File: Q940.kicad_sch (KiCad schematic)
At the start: 15 parts, among them J1 Power, J101 TO_HX711, J102 SHT-3x Temperature-1, J103 SHT-3x Temperature-2, J104 TO L298N MOTOR-DRIVER, J105 I2C LCD 16x2, J106 PWR_INPUT, J2 Digital/PWM, J3 Analog, J4 Digital/PWM

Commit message: とりあえずリリース
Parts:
- added C106: 0.1uF/50V, Capacitor_THT:C_Disc_D3.8mm_W2.6mm_P2.50mm, symbol Device:C_Small
- added D101: 1N4007, symbol Device:D_Filled
- added M101: Geared Motor_DC 5V/5rpm, symbol Motor:Motor_DC
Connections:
- net +5V: now also C106.1, D101.1 (K), M101.1 (+)
- net GND: now also C106.2, D101.2 (A), M101.2 (-)

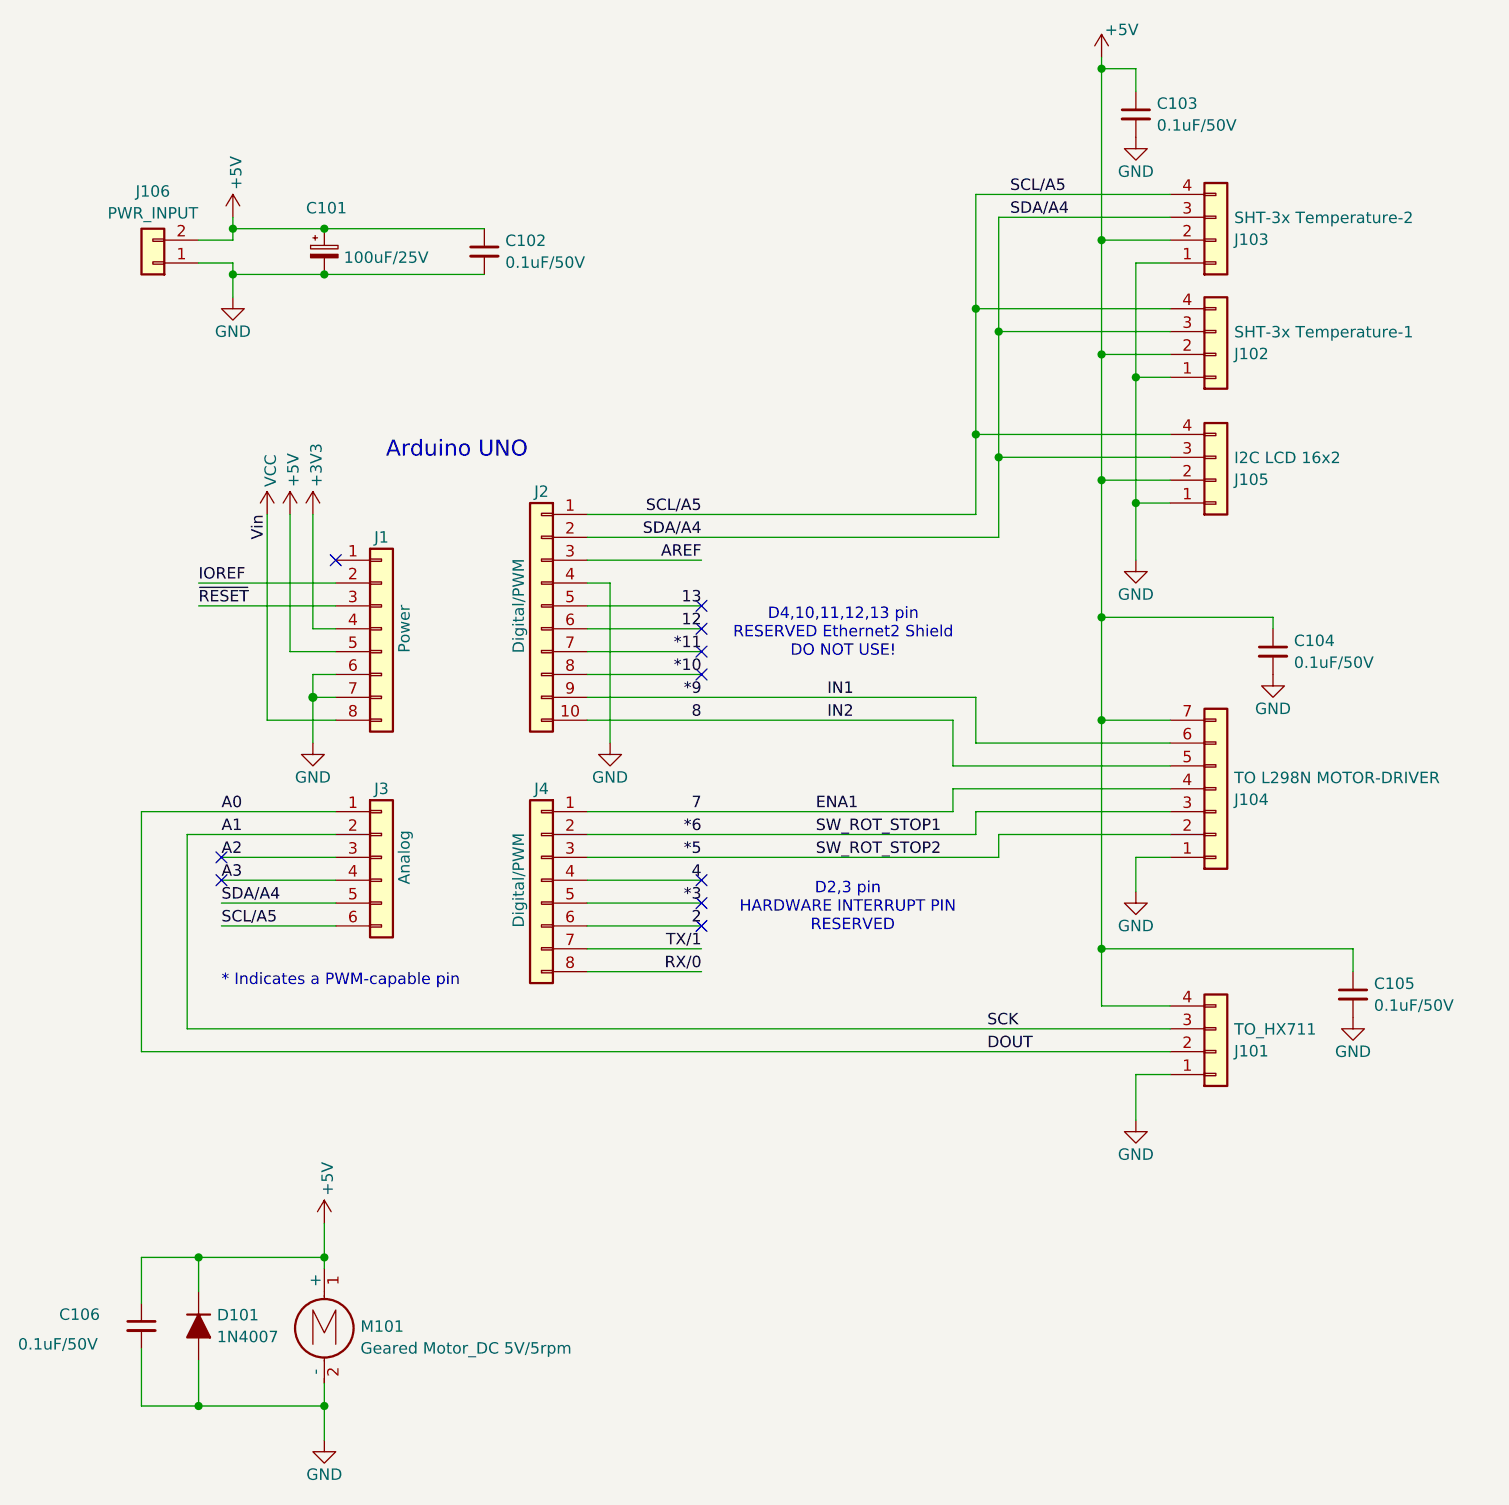
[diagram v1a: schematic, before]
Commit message: append MPU6050 and Hardware interruption
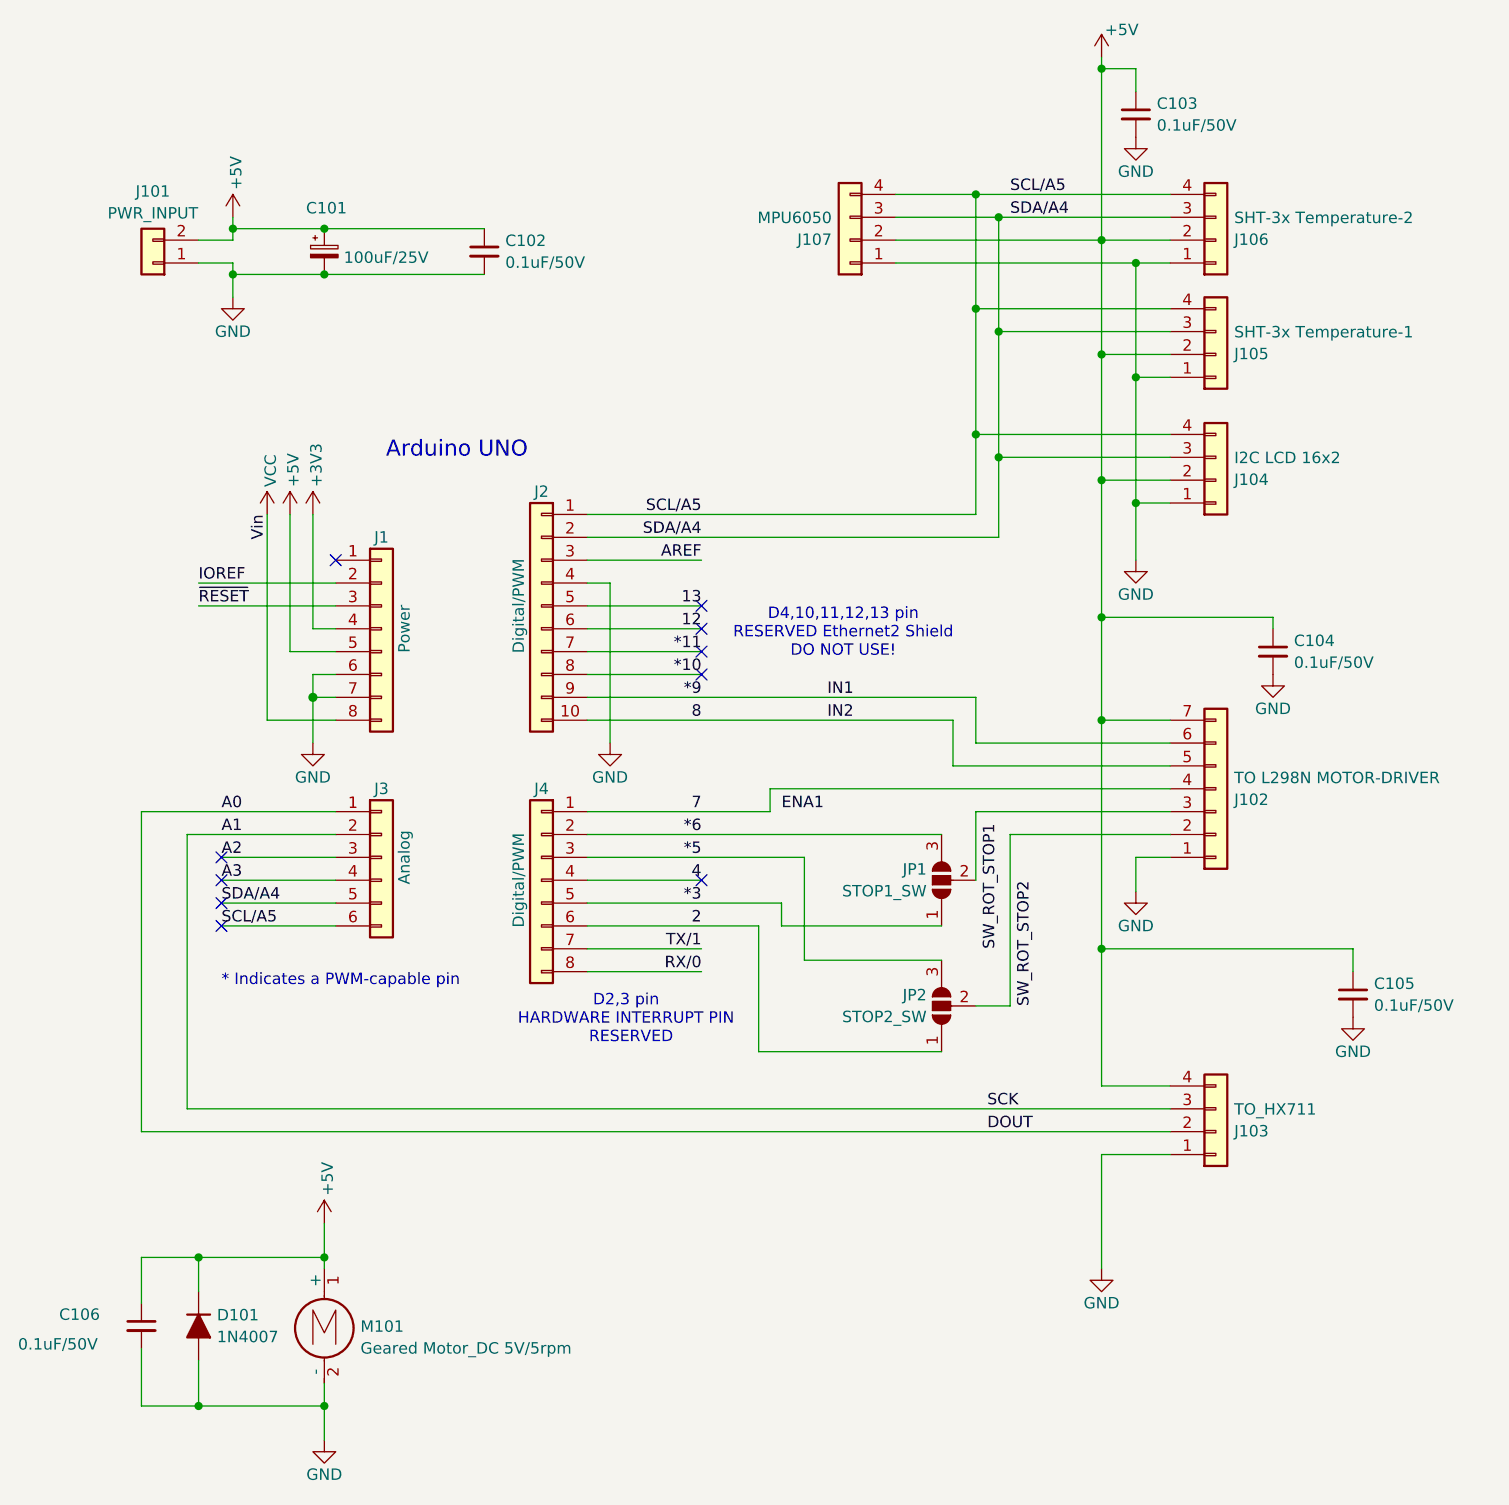
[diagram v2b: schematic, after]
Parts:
- added J107: MPU6050, Connector_JST:JST_XH_B4B-XH-A_1x04_P2.50mm_Vertical, symbol Connector_Generic:Conn_01x04
- added JP1: STOP1_SW, Jumper:SolderJumper-3_P1.3mm_Open_RoundedPad1.0x1.5mm_NumberLabels, symbol Jumper:SolderJumper_3_Open
- added JP2: STOP2_SW, Jumper:SolderJumper-3_P1.3mm_Open_RoundedPad1.0x1.5mm_NumberLabels, symbol Jumper:SolderJumper_3_Open
- J101: renamed from J106; footprint Connector_JST:JST_XH_B2B-XH-AM_1x02_P2.50mm_Vertical -> Connector_JST:JST_XH_B2B-XH-A_1x02_P2.50mm_Vertical
- J102: renamed from J104; footprint Connector_JST:JST_XH_B7B-XH-AM_1x07_P2.50mm_Vertical -> Connector_JST:JST_XH_B7B-XH-A_1x07_P2.50mm_Vertical
- J103: renamed from J101; footprint Connector_JST:JST_XH_B4B-XH-AM_1x04_P2.50mm_Vertical -> Connector_JST:JST_XH_B4B-XH-A_1x04_P2.50mm_Vertical
- J104: renamed from J105; footprint Connector_JST:JST_XH_B4B-XH-AM_1x04_P2.50mm_Vertical -> Connector_JST:JST_XH_B4B-XH-A_1x04_P2.50mm_Vertical
- J105: renamed from J102; footprint Connector_JST:JST_XH_B4B-XH-AM_1x04_P2.50mm_Vertical -> Connector_JST:JST_XH_B4B-XH-A_1x04_P2.50mm_Vertical
- J106: renamed from J103; footprint Connector_JST:JST_XH_B4B-XH-AM_1x04_P2.50mm_Vertical -> Connector_JST:JST_XH_B4B-XH-A_1x04_P2.50mm_Vertical
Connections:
- net *3: now also JP1.1 (A)
- net *5: now also JP2.3 (B); no longer J102.2 (Pin_2)
- net *6: now also JP1.3 (B); no longer J102.3 (Pin_3)
- net +5V: now also J107.2 (Pin_2)
- net 2: now also JP2.1 (A)
- net GND: now also J107.1 (Pin_1)
- net SCL/A5: now also J107.4 (Pin_4)
- net SDA/A4: now also J107.3 (Pin_3)
- new net: J102.2 (Pin_2), JP2.2 (C)
- new net: J102.3 (Pin_3), JP1.2 (C)
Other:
- moved on the sheet: J103

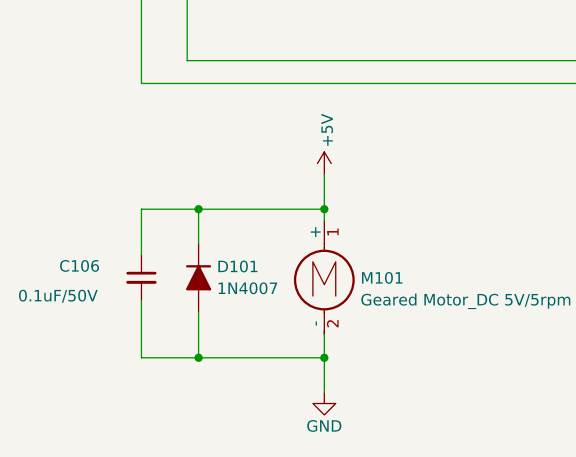
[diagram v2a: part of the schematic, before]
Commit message: remove 1N4007
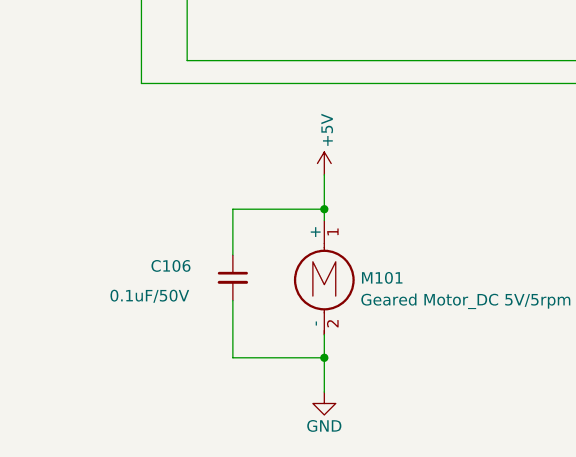
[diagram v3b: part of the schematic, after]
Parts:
- removed D101: 1N4007, symbol Device:D_Filled
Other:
- moved on the sheet: C106
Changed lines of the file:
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@@
-	)
-	(junction
-		(at 107.95 170.18)
-		(diameter 0)
-		(color 0 0 0 0)
 	)
 	(junction
@@
 	)
 	(junction
-		(at 107.95 153.67)
-		(diameter 0)
-		(color 0 0 0 0)
-	)
-	(junction
 		(at 208.28 40.64)
 		(diameter 0)
@@
 	(wire
 		(pts
-			(xy 107.95 153.67) (xy 121.92 153.67)
+			(xy 111.76 153.67) (xy 121.92 153.67)
 		)
 		(stroke
@@
 	(wire
 		(pts
-			(xy 107.95 153.67) (xy 101.6 153.67)
-		)
-		(stroke
-			(width 0)
-			(type default)
-		)
-	)
-	(wire
-		(pts
 			(xy 151.13 81.28) (xy 163.83 81.28)
 		)
@@
 	(wire
 		(pts
-			(xy 107.95 157.48) (xy 107.95 153.67)
-		)
-		(stroke
-			(width 0)
-			(type default)
-		)
-	)
-	(wire
-		(pts
 			(xy 190.5 120.65) (xy 175.26 120.65)
 		)
@@
 	(wire
 		(pts
-			(xy 107.95 165.1) (xy 107.95 170.18)
-		)
-		(stroke
-			(width 0)
-			(type default)
-		)
-	)
-	(wire
-		(pts
 			(xy 198.12 106.68) (xy 215.9 106.68)
 		)
@@
 	(wire
 		(pts
-			(xy 101.6 163.83) (xy 101.6 170.18)
+			(xy 111.76 163.83) (xy 111.76 170.18)
 		)
 		(stroke
@@
 	(wire
 		(pts
-			(xy 101.6 153.67) (xy 101.6 158.75)
+			(xy 111.76 153.67) (xy 111.76 158.75)
 		)
 		(stroke
@@
 	(wire
 		(pts
-			(xy 107.95 170.18) (xy 121.92 170.18)
-		)
-		(stroke
-			(width 0)
-			(type default)
-		)
-	)
-	(wire
-		(pts
 			(xy 196.85 50.8) (xy 215.9 50.8)
 		)
@@
 	(wire
 		(pts
-			(xy 101.6 170.18) (xy 107.95 170.18)
+			(xy 111.76 170.18) (xy 121.92 170.18)
 		)
 		(stroke
@@
 	)
 	(symbol
-		(lib_id "Device:D_Filled")
-		(at 107.95 161.29 270)
-		(unit 1)
-		(exclude_from_sim no)
-		(in_bom yes)
-		(on_board no)
-		(dnp no)
-		(fields_autoplaced yes)
-		(property "Reference" "D101"
-			(at 109.982 160.0778 90)
-			(effects
-				(font
-					(size 1.27 1.27)
-				)
-				(justify left)
-			)
-		)
-		(property "Value" "1N4007"
-			(at 109.982 162.5021 90)
-			(effects
-				(font
-					(size 1.27 1.27)
-				)
-				(justify left)
-			)
-		)
-		(property "Footprint" ""
-			(at 107.95 161.29 0)
-			(effects
-				(font
-					(size 1.27 1.27)
-				)
-				(hide yes)
-			)
-		)
-		(property "Datasheet" "~"
-			(at 107.95 161.29 0)
-			(effects
-				(font
-					(size 1.27 1.27)
-				)
-				(hide yes)
-			)
-		)
-		(property "Description" "Diode, filled shape"
-			(at 107.95 161.29 0)
-			(effects
-				(font
-					(size 1.27 1.27)
-				)
-				(hide yes)
-			)
-		)
-		(property "Sim.Device" "D"
-			(at 107.95 161.29 0)
-			(effects
-				(font
-					(size 1.27 1.27)
-				)
-				(hide yes)
-			)
-		)
-		(property "Sim.Pins" "1=K 2=A"
-			(at 107.95 161.29 0)
-			(effects
-				(font
-					(size 1.27 1.27)
-				)
-				(hide yes)
-			)
-		)
-		(pin "2"
-		)
-		(pin "1"
-		)
-		(instances
-			(project "Q940"
-				(path "/e63e39d7-6ac0-4ffd-8aa3-1841a4541b55"
-					(reference "D101")
-					(unit 1)
-				)
-			)
-		)
-	)
-	(symbol
 		(lib_id "power:GND")
 		(at 121.92 173.99 0)
@@
 	(symbol
 		(lib_id "Device:C_Small")
-		(at 101.6 161.29 0)
+		(at 111.76 161.29 0)
 		(unit 1)
 		(exclude_from_sim no)
@@
 		(dnp no)
 		(property "Reference" "C106"
-			(at 92.456 160.02 0)
+			(at 102.616 160.02 0)
 			(effects
 				(font
@@
 		)
 		(property "Value" "0.1uF/50V"
-			(at 87.884 163.322 0)
+			(at 98.044 163.322 0)
 			(effects
 				(font
@@
 		)
 		(property "Footprint" "Capacitor_THT:C_Disc_D3.8mm_W2.6mm_P2.50mm"
-			(at 101.6 161.29 0)
+			(at 111.76 161.29 0)
 			(effects
 				(font
@@
 		)
 		(property "Datasheet" "~"
-			(at 101.6 161.29 0)
+			(at 111.76 161.29 0)
 			(effects
 				(font
@@
 		)
 		(property "Description" "Unpolarized capacitor, small symbol"
-			(at 101.6 161.29 0)
-			(effects
-				(font
+			(at 111.76 161.29 0)
+			(effects
+				(font
